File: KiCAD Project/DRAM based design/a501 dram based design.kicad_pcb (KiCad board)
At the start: 2 copper layers, 58.4 x 73.7 mm, 65 parts, among them J1 Conn_02x28_Odd_Even, U1 M11B416256A-35TG, U2 M11B416256A-35TG

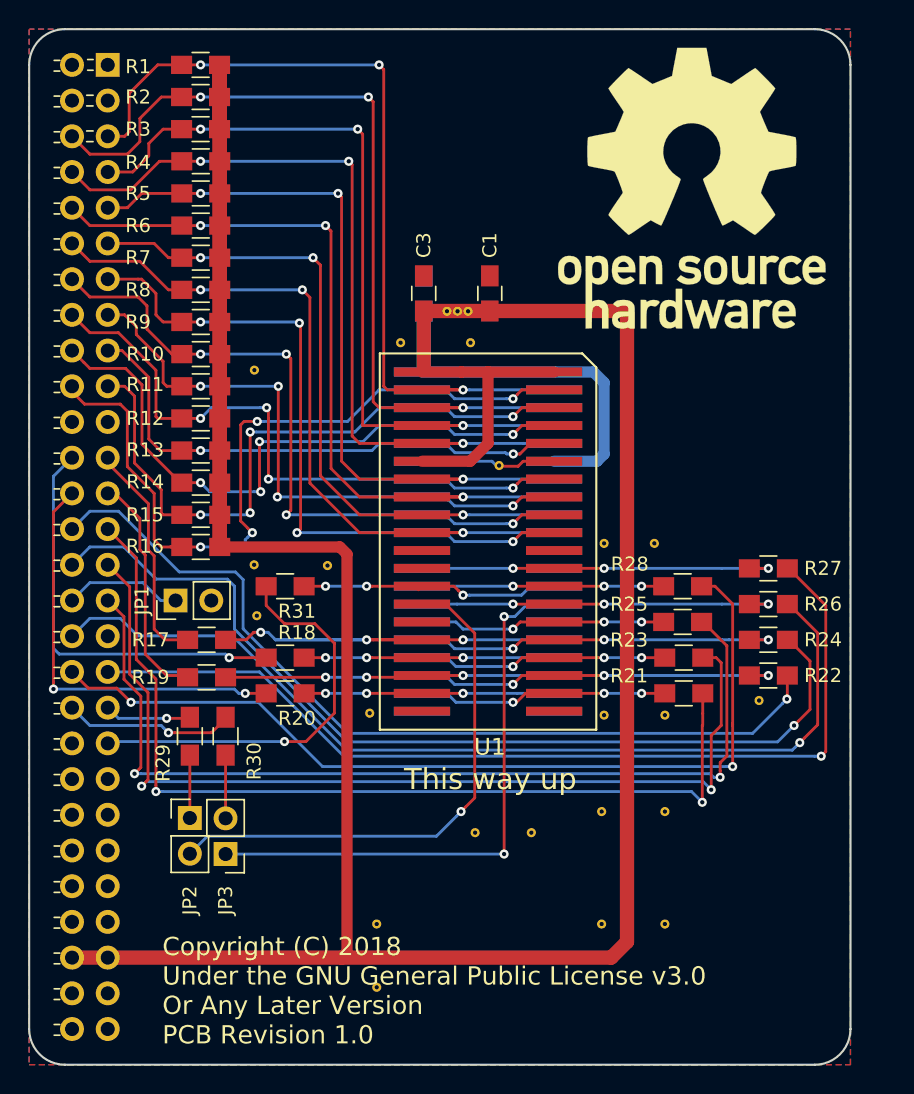
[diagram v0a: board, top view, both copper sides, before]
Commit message: Adding the completed keypad prototype kicad files. Finished a long time ago, just forgot to push
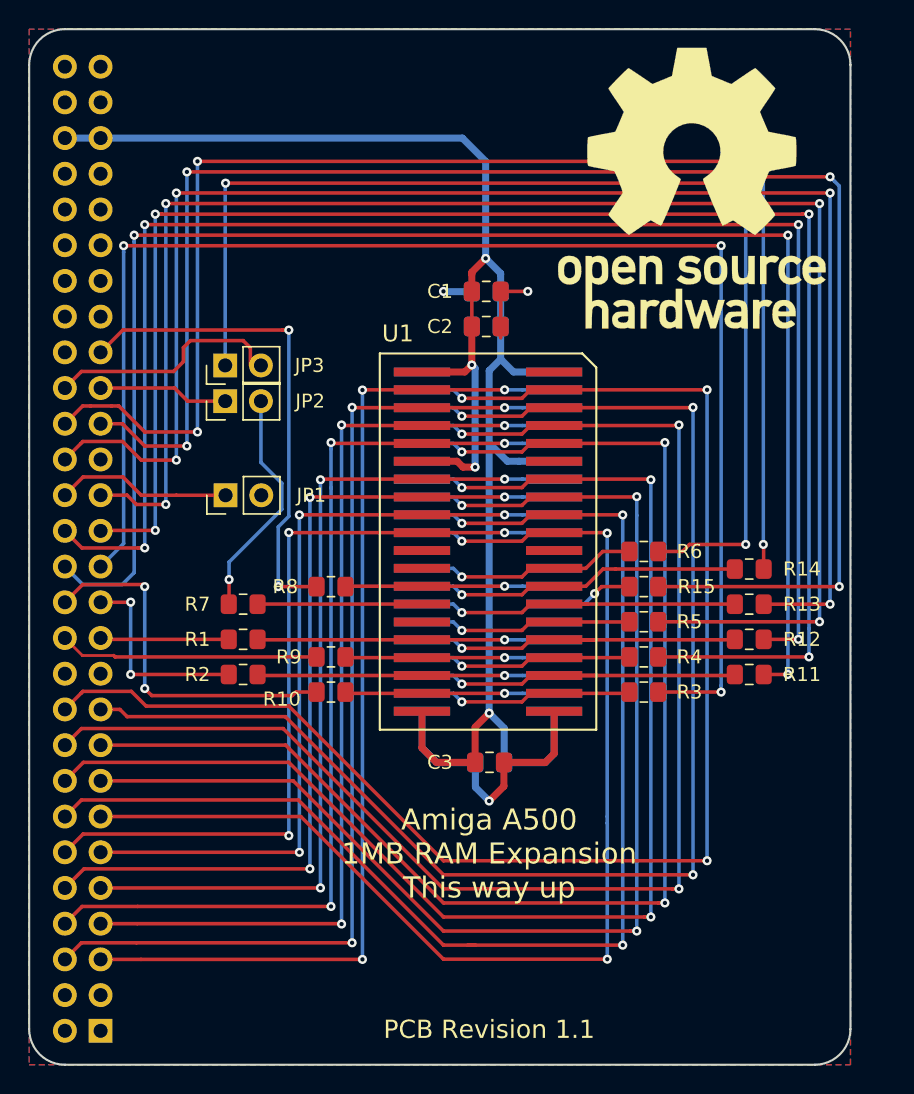
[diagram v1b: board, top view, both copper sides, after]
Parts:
- removed R16, R17, R18, R19, R20, R21, R22, R23, R24, R25, R26, R27, R28, R29, R30, R31: 4K7, Resistors_SMD:R_0805_HandSoldering
- removed REF** (x24): VIA-0.3mm-drill-0.65mm-diameter, Amiga_RAM:VIA-0.3mm-drill-0.65mm-diameter
- added C4: 10u, Capacitor_SMD:C_0805_2012Metric_Pad1.15x1.40mm_HandSolder, B.Cu at (177.3, 72.5)
- added C5: 10n, Capacitor_SMD:C_0805_2012Metric_Pad1.15x1.40mm_HandSolder, B.Cu at (177.3, 75.0)
- added C6: 10n, Capacitor_SMD:C_0805_2012Metric_Pad1.15x1.40mm_HandSolder, B.Cu at (177.5, 106.0)
- C1, C3: footprint Capacitors_SMD:C_0805_HandSoldering -> Capacitor_SMD:C_0805_2012Metric_Pad1.15x1.40mm_HandSolder
- C2: footprint Capacitors_SMD:C_0805_HandSoldering -> Capacitor_SMD:C_0805_2012Metric_Pad1.15x1.40mm_HandSolder; moved to F.Cu
- J1: moved to B.Cu
- R1, R10, R11, R12, R13, R14, R15, R2, R3, R4, R5, R6, R7, R8, R9: footprint Resistors_SMD:R_0805_HandSoldering -> Resistor_SMD:R_0805_2012Metric_Pad1.15x1.40mm_HandSolder
- moved J1 68.7 mm to (147.3, 125.1)
- moved R3 51.0 mm to (188.5, 101.0)
- moved R4 47.3 mm to (188.5, 98.5)
- moved R11 44.1 mm to (196.0, 99.8), turned to 180 degrees
- moved R5 43.8 mm to (188.5, 96.0)
- moved R12 42.1 mm to (196.0, 97.2), turned to 180 degrees
- moved R2 41.2 mm to (160.0, 99.8), turned to 180 degrees
- moved R1 41.0 mm to (160.0, 97.2), turned to 180 degrees
- moved R13 40.5 mm to (196.0, 94.8), turned to 180 degrees
- moved R14 39.5 mm to (196.0, 92.2), turned to 180 degrees
- moved R6 39.1 mm to (188.5, 91.0)
- moved JP3 34.8 mm to (158.7, 77.8), turned to 90 degrees
- moved C3 33.7 mm to (177.5, 106.0), turned to 0 degrees
- moved R15 31.9 mm to (188.5, 93.5), turned to 180 degrees
- moved JP2 29.8 mm to (158.7, 80.3), turned to 90 degrees
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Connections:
- J1 pad 37: Net-(J1-Pad37) -> /~RAS0
- J1 pad 38: Net-(J1-Pad38) -> /~RAS1
- JP2 pad 2: /~RAS0out -> Net-(JP2-Pad2)
- JP3 pad 1: /~RAS1out -> Net-(JP3-Pad1)
- R1 pad 1: /DQ0 -> /A0
- R1 pad 2: +5V -> Net-(J1-Pad23)
- R10 pad 1: /DQ9 -> Net-(J1-Pad26)
- R10 pad 2: +5V -> /A3
- R11 pad 1: /DQ10 -> Net-(J1-Pad28)
- R11 pad 2: +5V -> /A5
- R12 pad 1: /DQ11 -> Net-(J1-Pad30)
- R12 pad 2: +5V -> /A7
- R13 pad 1: /DQ12 -> Net-(J1-Pad34)
- R13 pad 2: +5V -> /~OE
- R14 pad 1: /DQ13 -> Net-(J1-Pad36)
- R14 pad 2: +5V -> /~CASU
- R15 pad 1: /DQ14 -> Net-(JP3-Pad1)
- R15 pad 2: +5V -> /~RAS1out
- R2 pad 1: /DQ1 -> /A2
- R2 pad 2: +5V -> Net-(J1-Pad25)
- R3 pad 1: /DQ2 -> /A4
- R3 pad 2: +5V -> Net-(J1-Pad27)
- R4 pad 1: /DQ3 -> /A6
- R4 pad 2: +5V -> Net-(J1-Pad29)
- R5 pad 1: /DQ4 -> /A8
- R5 pad 2: +5V -> Net-(J1-Pad31)
- R6 pad 1: /DQ5 -> /~CASL
- R6 pad 2: +5V -> Net-(J1-Pad35)
- R7 pad 1: /DQ6 -> Net-(JP2-Pad2)
- R7 pad 2: +5V -> /~RAS0out
- R8 pad 1: /DQ7 -> /~WE
- R8 pad 2: +5V -> Net-(J1-Pad39)
- R9 pad 1: /DQ8 -> Net-(J1-Pad24)
- R9 pad 2: +5V -> /A1
- U1 pad 20: GND -> +5V
- U1 pad 40: +5V -> GND
- U2 pad 20: GND -> +5V
- U2 pad 40: +5V -> GND
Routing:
- net +5V: track 276.3 -> 125.6 mm, vias 0 -> 4
- net Net-(JP3-Pad1): track 0.00 -> 98.5 mm, vias 0 -> 3
- net /DQ12: track 38.1 -> 93.7 mm, vias 2 -> 3
- net /DQ13: track 45.6 -> 99.0 mm, vias 4 -> 3
- net /DQ14: track 46.6 -> 98.4 mm, vias 4 -> 3
- net /DQ11: track 45.1 -> 93.0 mm, vias 4 -> 3
- net Net-(J1-Pad31): track 67.3 -> 114.0 mm, vias 2 -> 4
- net /DQ15: track 57.1 -> 103.8 mm, vias 4 -> 3
- net Net-(J1-Pad28): track 62.7 -> 109.3 mm, vias 1 -> 3
- net Net-(J1-Pad29): track 68.9 -> 115.1 mm, vias 2 -> 4
- net /DQ10: track 43.6 -> 87.6 mm, vias 4 -> 3
- net Net-(J1-Pad34): track 67.7 -> 108.5 mm, vias 1 -> 4
- net Net-(J1-Pad30): track 67.2 -> 107.7 mm, vias 1 -> 4
- net /DQ9: track 51.4 -> 88.6 mm, vias 4 -> 3
- net Net-(J1-Pad27): track 67.0 -> 102.2 mm, vias 2 -> 3
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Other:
- net class Default: clearance 0.2032 -> 0.1524; trace_width 0.2032 -> 0.1524
- rule pad_to_mask_clearance: 0.2 -> 0.1016
- rule trace_clearance: 0.2032 -> 0.1524
- rule trace_min: 0.2032 -> 0.1524
- board text added: "Amiga A500 1MB RAM Expansion This way up"
- board text added: "PCB Revision 1.1"
- board text removed: "Copyright (C) 2018 Under the GNU General Public License v3.0 Or Any Later Version PCB Revision 1.0"
- board text removed: "This way down"
- board text removed: "This way up"
